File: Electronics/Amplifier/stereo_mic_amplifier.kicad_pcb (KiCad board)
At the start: 2 copper layers, 26 parts, among them P1 mic_L, P2 mic_R, P3 batt, P4 CONN_01X03, U1 TL072

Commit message: Fixed dual potentiometer pins
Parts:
- moved C1 217.8 mm to (-87.6, 106.7)
- moved R8 211.6 mm to (-108.0, 125.7)
- moved C2 203.9 mm to (-77.5, 83.8)
- moved C5 186.3 mm to (-69.8, 40.6)
- moved C8 184.6 mm to (229.9, 111.8), turned to 180 degrees
- moved C3 184.5 mm to (229.9, 95.2), turned to 270 degrees
- moved C4 177.8 mm to (-66.0, 58.4)
- moved P4 174.1 mm to (-100.3, 27.9), turned to 270 degrees
- moved C7 171.5 mm to (257.8, 87.6), turned to 270 degrees
- moved U1 156.9 mm to (250.2, 90.2)
- moved R3 156.5 mm to (237.5, 85.1), turned to 270 degrees
- moved R4 145.3 mm to (240.0, 95.2), turned to 270 degrees
- moved R5 144.9 mm to (241.3, 111.8)
- moved R1 134.9 mm to (-8.89, 57.1)
- moved P2 129.2 mm to (-55.9, 125.7), turned to 270 degrees
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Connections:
- D1 pad 2: Net-(D1-Pad2) -> GND
- P3 pad 1: Net-(D1-Pad2) -> GND
- RV1 pad 11: (no net) -> pot_a_L
- RV1 pad 12: (no net) -> pot_b_L
- RV1 pad 21: (no net) -> pot_a_R
- RV1 pad 22: (no net) -> pot_b_R

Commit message: Deciding layout
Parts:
- moved P4 256.3 mm to (132.1, 135.9)
- moved C1 191.5 mm to (100.3, 69.8), turned to 90 degrees
- moved C3 188.6 mm to (44.5, 129.5)
- moved C2 185.9 mm to (99.1, 142.2), turned to 270 degrees
- moved R8 176.6 mm to (68.6, 121.9), turned to 90 degrees
- moved R6 173.4 mm to (72.4, 108.0), turned to 270 degrees
- moved C7 169.7 mm to (88.4, 97.5), turned to 0 degrees
- moved R5 169.2 mm to (72.4, 121.9), turned to 90 degrees
- moved C8 167.0 mm to (63.2, 123.2), turned to 270 degrees
- moved R4 166.0 mm to (76.2, 121.9)
- moved U1 164.5 mm to (86.4, 105.4)
- moved R3 162.9 mm to (76.2, 108.0)
- moved C9 162.7 mm to (69.8, 97.8)
- moved C5 161.0 mm to (80.8, 97.5)
- moved C4 158.5 mm to (82.8, 113.0)
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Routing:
- net vgnd: track 0.00 -> 28.5 mm
- net +9V: track 0.00 -> 25.8 mm
- net pot_b_R: track 0.00 -> 25.4 mm
- net pot_b_L: track 0.00 -> 17.9 mm
- net GND: track 0.00 -> 17.1 mm
- net Net-(C8-Pad1): track 0.00 -> 11.5 mm
- net L_out: track 0.00 -> 6.39 mm
- net Net-(C9-Pad1): track 0.00 -> 5.61 mm
- net R_out: track 0.00 -> 5.08 mm
- net pot_a_L: track 0.00 -> 4.93 mm
- net pot_a_R: track 0.00 -> 4.83 mm
- net Net-(D2-Pad1): track 0.00 -> 3.81 mm
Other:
- net class Default: clearance 0.2 -> 0.3; trace_width 0.25 -> 0.7; via_dia 0.6 -> 1.6; via_drill 0.4 -> 0.8
- rule trace_clearance: 0.2 -> 0.3

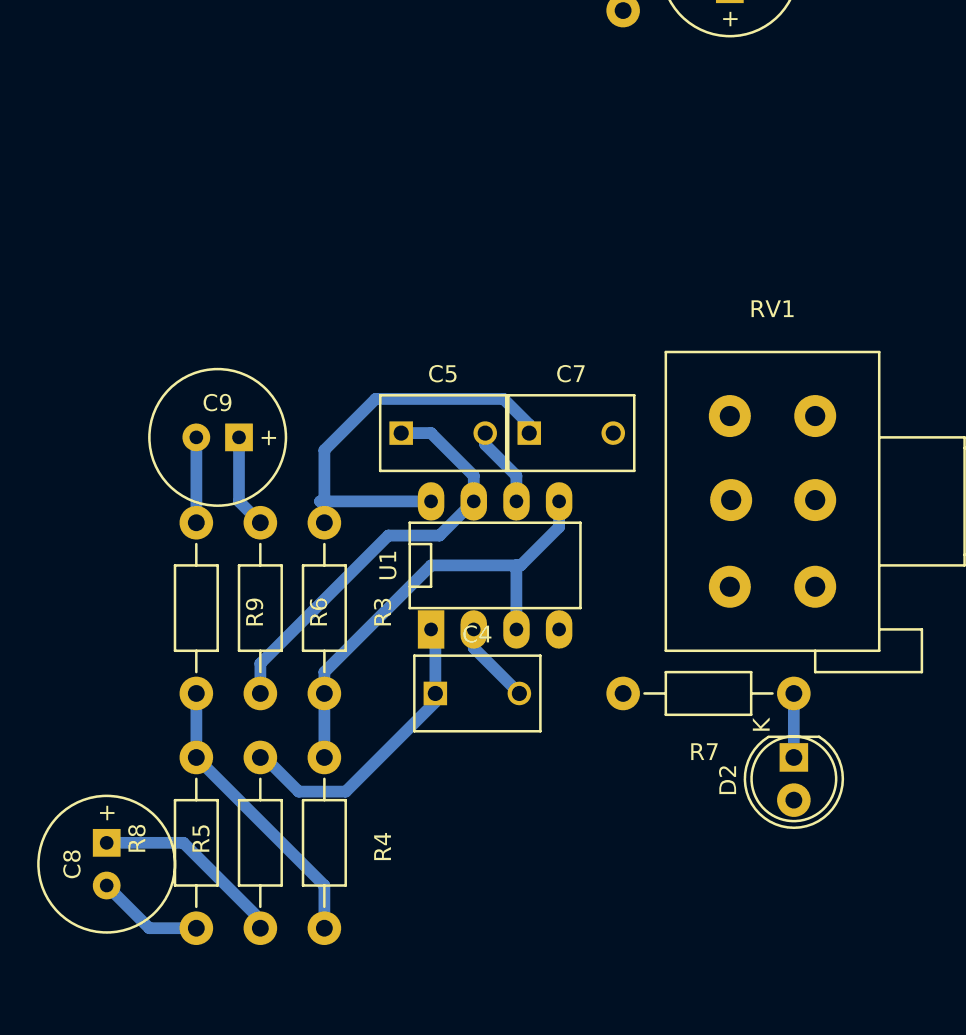
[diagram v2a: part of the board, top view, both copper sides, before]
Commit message: Fixing kicad libraries
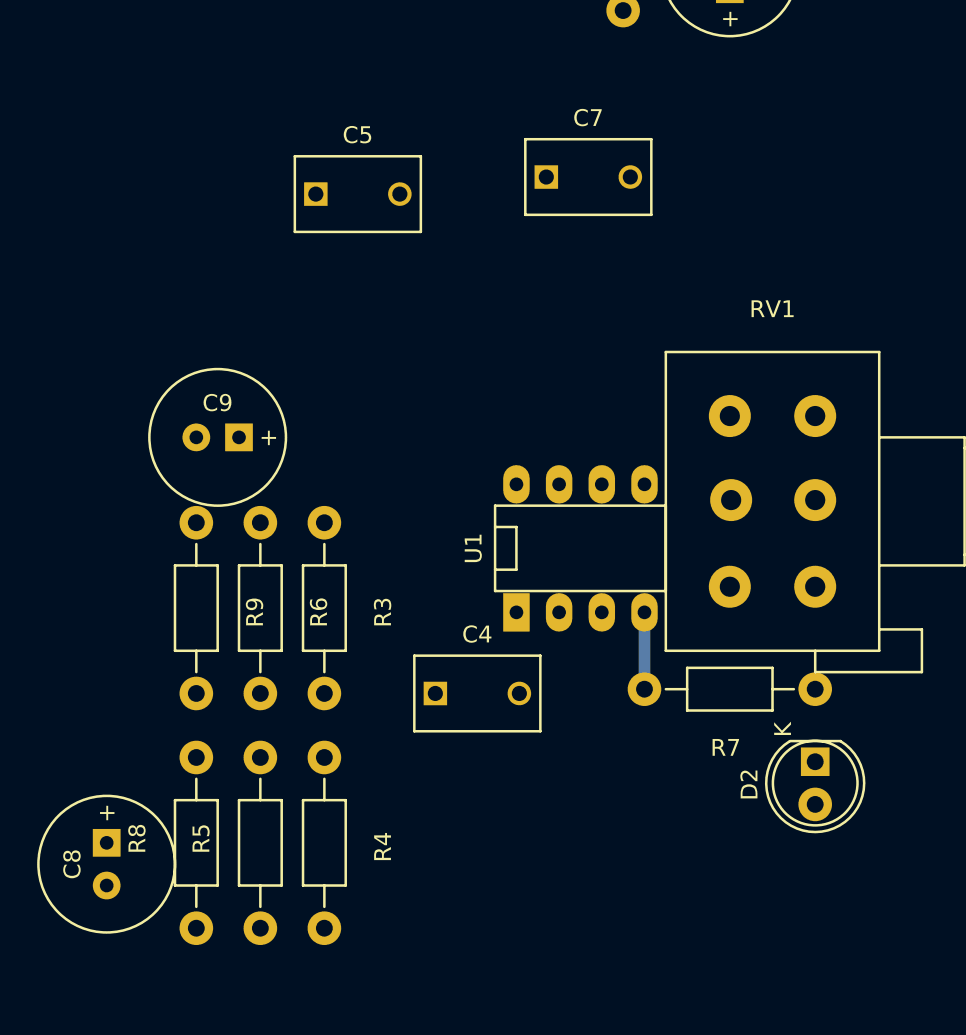
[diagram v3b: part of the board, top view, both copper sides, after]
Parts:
- moved C7 15.3 mm to (89.4, 82.3)
- moved C5 15.1 mm to (75.7, 83.3)
- moved U1 5.18 mm to (91.4, 104.4)
- moved R7 1.30 mm to (100.3, 112.8)
- moved D2 1.30 mm to (105.4, 117.1)
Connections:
- RV1 pad 11: pot_a_L -> (no net)
- RV1 pad 12: pot_b_L -> (no net)
- RV1 pad 21: pot_a_R -> (no net)
- RV1 pad 22: pot_b_R -> (no net)
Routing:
- net vgnd: track 28.5 -> 0.00 mm
- net +9V: track 25.8 -> 0.00 mm
- net pot_b_R: track 25.4 -> 0.00 mm
- net pot_b_L: track 17.9 -> 0.00 mm
- net GND: track 17.1 -> 4.57 mm
- net Net-(C8-Pad1): track 11.5 -> 0.00 mm
- net L_out: track 6.39 -> 0.00 mm
- net Net-(C9-Pad1): track 5.61 -> 0.00 mm
- net R_out: track 5.08 -> 0.00 mm
- net pot_a_L: track 4.93 -> 0.00 mm
- net pot_a_R: track 4.83 -> 0.00 mm
- net Net-(D2-Pad1): track 3.81 -> 0.00 mm
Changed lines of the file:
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@@
 (kicad_pcb (version 4) (host pcbnew "(after 2015-mar-04 BZR unknown)-product")
   (general
-    (links 47)
-    (no_connects 29)
-    (area 27.134999 60.154999 140.388334 151.935001)
+    (links 43)
+    (no_connects 42)
+    (area 0 0 0 0)
     (thickness 1.6)
     (drawings 0)
-    (tracks 50)
+    (tracks 1)
     (zones 0)
     (modules 26)
@@
   )
   (module Capacitors_ThroughHole:C_Disc_D7.5_P5 (layer F.Cu)
-    (at 80.772 97.536)
+    (at 75.692 83.312)
     (descr "Capacitor 7.5mm Disc, Pitch 5mm")
     (tags Capacitor)
@@
   )
   (module Capacitors_ThroughHole:C_Disc_D7.5_P5 (layer F.Cu)
-    (at 88.392 97.536)
+    (at 89.408 82.296)
     (descr "Capacitor 7.5mm Disc, Pitch 5mm")
     (tags Capacitor)
@@
   )
   (module LEDs:LED-5MM (layer F.Cu)
-    (at 104.14 116.84 270)
+    (at 105.41 117.094 270)
     (descr "LED vertical 5mm")
     (tags "LED-5MM LED 5mm")
@@
   )
   (module Resistors_ThroughHole:Resistor_Horizontal_RM10mm (layer F.Cu)
-    (at 99.06 113.03 180)
+    (at 100.33 112.776 180)
     (descr "Resistor, Axial,  RM 10mm, 1/3W,")
     (tags "Resistor, Axial, RM 10mm, 1/3W,")
@@
     (fp_line (start 3.81 -13.97) (end 3.81 3.81) (layer F.SilkS) (width 0.15))
     (pad 23 thru_hole circle (at -5.08 -10.16) (size 2.49936 2.49936) (drill 1.19888) (layers *.Cu *.Mask F.SilkS))
-    (pad 22 thru_hole circle (at -5.00126 -5.15874) (size 2.49936 2.49936) (drill 1.19888) (layers *.Cu *.Mask F.SilkS)
-      (net 8 pot_b_R))
-    (pad 21 thru_hole circle (at -5.08 0) (size 2.49936 2.49936) (drill 1.19888) (layers *.Cu *.Mask F.SilkS)
-      (net 4 pot_a_R))
-    (pad 12 thru_hole circle (at 0 -5.15874) (size 2.49936 2.49936) (drill 1.19888) (layers *.Cu *.Mask F.SilkS)
-      (net 7 pot_b_L))
+    (pad 22 thru_hole circle (at -5.00126 -5.15874) (size 2.49936 2.49936) (drill 1.19888) (layers *.Cu *.Mask F.SilkS))
+    (pad 21 thru_hole circle (at -5.08 0) (size 2.49936 2.49936) (drill 1.19888) (layers *.Cu *.Mask F.SilkS))
+    (pad 12 thru_hole circle (at 0 -5.15874) (size 2.49936 2.49936) (drill 1.19888) (layers *.Cu *.Mask F.SilkS))
     (pad 13 thru_hole circle (at 0 -10.16) (size 2.49936 2.49936) (drill 1.19888) (layers *.Cu *.Mask F.SilkS))
-    (pad 11 thru_hole circle (at 0 0) (size 2.49936 2.49936) (drill 1.19888) (layers *.Cu *.Mask F.SilkS)
-      (net 2 pot_a_L))
+    (pad 11 thru_hole circle (at 0 0) (size 2.49936 2.49936) (drill 1.19888) (layers *.Cu *.Mask F.SilkS))
     (model Potentiometers.3dshapes/Potentiometer_Alps-RK163-double_15mm.wrl
       (at (xyz 0 0 0))
@@
   )
   (module Sockets_DIP:DIP-8__300_ELL (layer F.Cu)
-    (at 86.36 105.41)
+    (at 91.44 104.394)
     (descr "8 pins DIL package, elliptical pads")
     (tags DIL)
@@
     )
   )
-  (segment (start 85.09 109.22) (end 85.09 110.316) (width 0.7) (layer B.Cu) (net 2))
-  (segment (start 85.09 110.316) (end 87.804 113.03) (width 0.7) (layer B.Cu) (net 2))
-  (segment (start 85.772 97.536) (end 85.772 98.218) (width 0.7) (layer B.Cu) (net 4))
-  (segment (start 85.772 98.218) (end 87.63 100.076) (width 0.7) (layer B.Cu) (net 4))
-  (segment (start 87.63 100.076) (end 87.63 101.6) (width 0.7) (layer B.Cu) (net 4))
-  (segment (start 76.2 127) (end 76.2 124.46) (width 0.7) (layer B.Cu) (net 5))
-  (segment (start 76.2 124.46) (end 68.58 116.84) (width 0.7) (layer B.Cu) (net 5))
-  (segment (start 68.58 116.84) (end 68.58 113.03) (width 0.7) (layer B.Cu) (net 5))
-  (segment (start 87.63 109.22) (end 87.63 105.41) (width 0.7) (layer B.Cu) (net 6))
-  (segment (start 87.63 105.41) (end 87.63 105.664) (width 0.7) (layer B.Cu) (net 6))
-  (segment (start 87.63 105.664) (end 87.63 105.41) (width 0.7) (layer B.Cu) (net 6))
-  (segment (start 76.2 113.03) (end 76.2 111.76) (width 0.7) (layer B.Cu) (net 6))
-  (segment (start 90.17 103.124) (end 90.17 101.6) (width 0.7) (layer B.Cu) (net 6))
-  (segment (start 87.884 105.41) (end 90.17 103.124) (width 0.7) (layer B.Cu) (net 6))
-  (segment (start 82.55 105.41) (end 87.63 105.41) (width 0.7) (layer B.Cu) (net 6))
-  (segment (start 87.63 105.41) (end 87.884 105.41) (width 0.7) (layer B.Cu) (net 6))
-  (segment (start 76.2 111.76) (end 82.55 105.41) (width 0.7) (layer B.Cu) (net 6))
-  (segment (start 76.2 116.84) (end 76.2 113.03) (width 0.7) (layer B.Cu) (net 6))
-  (segment (start 72.39 116.84) (end 72.644 116.84) (width 0.7) (layer B.Cu) (net 7))
-  (segment (start 72.644 116.84) (end 74.676 118.872) (width 0.7) (layer B.Cu) (net 7))
-  (segment (start 74.676 118.872) (end 77.47 118.872) (width 0.7) (layer B.Cu) (net 7))
-  (segment (start 77.47 118.872) (end 82.804 113.538) (width 0.7) (layer B.Cu) (net 7))
-  (segment (start 82.804 113.538) (end 82.804 113.03) (width 0.7) (layer B.Cu) (net 7))
-  (segment (start 82.804 113.03) (end 82.804 109.474) (width 0.7) (layer B.Cu) (net 7))
-  (segment (start 82.804 109.474) (end 82.55 109.22) (width 0.7) (layer B.Cu) (net 7))
-  (segment (start 72.39 113.03) (end 72.39 111.252) (width 0.7) (layer B.Cu) (net 8))
-  (segment (start 83.058 103.632) (end 85.09 101.6) (width 0.7) (layer B.Cu) (net 8))
-  (segment (start 80.01 103.632) (end 83.058 103.632) (width 0.7) (layer B.Cu) (net 8))
-  (segment (start 72.39 111.252) (end 80.01 103.632) (width 0.7) (layer B.Cu) (net 8))
-  (segment (start 85.09 101.6) (end 85.09 100.076) (width 0.7) (layer B.Cu) (net 8))
-  (segment (start 82.55 97.536) (end 80.772 97.536) (width 0.7) (layer B.Cu) (net 8))
-  (segment (start 85.09 100.076) (end 82.55 97.536) (width 0.7) (layer B.Cu) (net 8))
-  (segment (start 82.55 101.6) (end 76.2 101.6) (width 0.7) (layer B.Cu) (net 9))
-  (segment (start 76.2 101.6) (end 75.946 101.6) (width 0.7) (layer B.Cu) (net 9))
-  (segment (start 75.946 101.6) (end 76.2 101.6) (width 0.7) (layer B.Cu) (net 9))
-  (segment (start 88.392 97.536) (end 88.392 97.028) (width 0.7) (layer B.Cu) (net 9))
-  (segment (start 88.392 97.028) (end 86.868 95.504) (width 0.7) (layer B.Cu) (net 9))
-  (segment (start 86.868 95.504) (end 79.248 95.504) (width 0.7) (layer B.Cu) (net 9))
-  (segment (start 79.248 95.504) (end 76.2 98.552) (width 0.7) (layer B.Cu) (net 9))
-  (segment (start 76.2 98.552) (end 76.2 101.6) (width 0.7) (layer B.Cu) (net 9))
-  (segment (start 76.2 101.6) (end 76.2 102.87) (width 0.7) (layer B.Cu) (net 9))
-  (segment (start 68.58 127) (end 65.786 127) (width 0.7) (layer B.Cu) (net 10) (status 400000))
-  (segment (start 65.786 127) (end 63.246 124.46) (width 0.7) (layer B.Cu) (net 10) (status 800000))
-  (segment (start 72.39 127) (end 72.39 126.492) (width 0.7) (layer B.Cu) (net 11) (status C00000))
-  (segment (start 72.39 126.492) (end 67.818 121.92) (width 0.7) (layer B.Cu) (net 11) (status 400000))
-  (segment (start 67.818 121.92) (end 63.246 121.92) (width 0.7) (layer B.Cu) (net 11) (status 800000))
-  (segment (start 68.58 102.87) (end 68.58 97.79) (width 0.7) (layer B.Cu) (net 12))
-  (segment (start 71.12 97.79) (end 71.12 101.6) (width 0.7) (layer B.Cu) (net 13))
-  (segment (start 71.12 101.6) (end 72.39 102.87) (width 0.7) (layer B.Cu) (net 13))
-  (segment (start 104.14 116.83866) (end 104.14 113.03) (width 0.7) (layer B.Cu) (net 14))
+  (segment (start 95.25 108.204) (end 95.25 112.776) (width 0.7) (layer B.Cu) (net 5))
 )

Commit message: Work on the layout
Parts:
- RV1: value Dual A100K -> DUAL_POT_OK
- moved C8 74.8 mm to (138.0, 120.7)
- moved R8 66.1 mm to (134.5, 127.0), turned to 180 degrees
- moved C9 64.6 mm to (120.8, 137.5), turned to 0 degrees
- moved R9 60.7 mm to (124.7, 131.1), turned to 0 degrees
- moved R5 49.2 mm to (121.2, 115.6)
- moved P3 48.1 mm to (75.7, 121.4), turned to 90 degrees
- moved R6 47.5 mm to (112.6, 133.1), turned to 90 degrees
- moved D1 43.8 mm to (76.8, 118.2), turned to 0 degrees
- moved C3 41.1 mm to (77.3, 104.9), turned to 180 degrees
- moved R1 39.8 mm to (81.9, 105.3)
- moved C6 37.0 mm to (77.3, 112.5), turned to 180 degrees
- moved C1 35.8 mm to (77.3, 97.3), turned to 180 degrees
- moved P1 34.4 mm to (86.5, 93.7)
- moved C7 34.0 mm to (86.9, 116.2), turned to 90 degrees
- moved C5 32.3 mm to (91.9, 111.3), turned to 270 degrees
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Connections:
- D2 pad 1: Net-(D2-Pad1) -> GND
- D2 pad 2: +9V -> Net-(D2-Pad2)
- R7 pad 1: Net-(D2-Pad1) -> +9V
- R7 pad 2: GND -> Net-(D2-Pad2)
- RV1 pad 12: (no net) -> pot_b_L
- RV1 pad 13: (no net) -> pot_a_L
- RV1 pad 22: (no net) -> pot_b_R
- RV1 pad 23: (no net) -> pot_a_R
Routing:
- net +9V: track 0.00 -> 60.4 mm
- net GND: track 4.57 -> 56.1 mm
- net pot_a_L: track 0.00 -> 40.0 mm
- net pot_a_R: track 0.00 -> 34.9 mm
- net vgnd: track 0.00 -> 21.7 mm
- net pot_b_L: track 0.00 -> 20.6 mm
- net pot_b_R: track 0.00 -> 17.4 mm
- net Net-(C1-Pad2): track 0.00 -> 15.7 mm
- net Net-(C2-Pad2): track 0.00 -> 12.6 mm
- net Net-(D2-Pad2): track 0.00 -> 4.83 mm

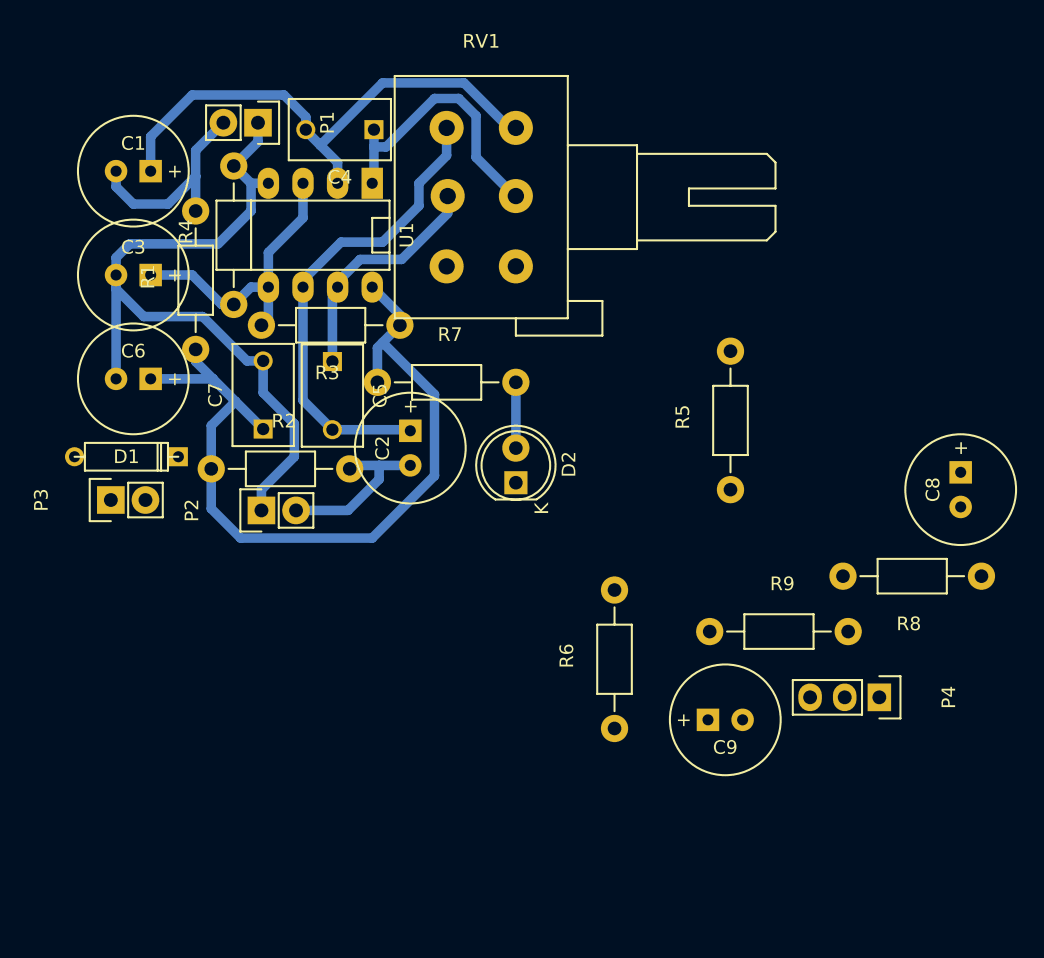
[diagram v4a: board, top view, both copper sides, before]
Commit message: Increased pad sizes & improvements in layout
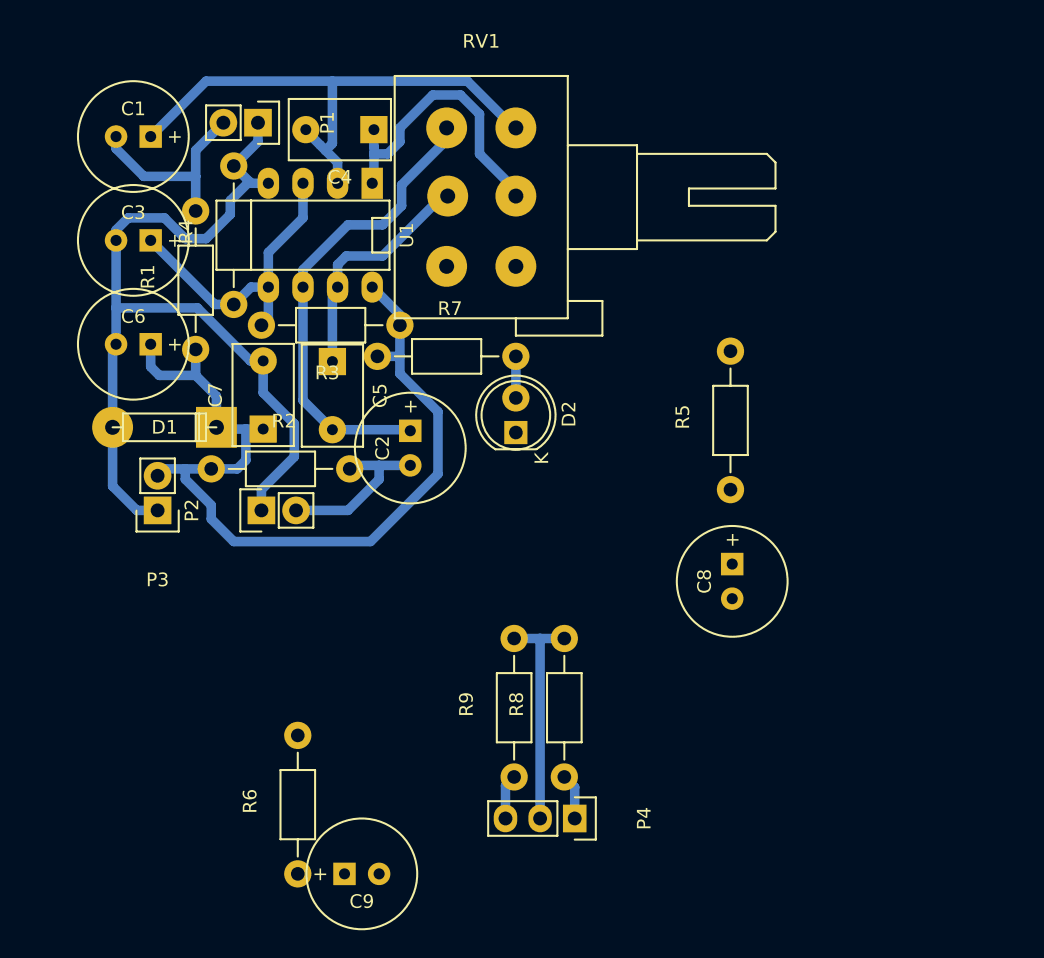
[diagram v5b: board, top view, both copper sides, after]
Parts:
- moved C9 29.0 mm to (94.1, 148.8)
- moved R8 27.3 mm to (109.0, 136.7), turned to 90 degrees
- moved R6 25.6 mm to (89.4, 143.8)
- moved P4 24.1 mm to (109.7, 144.8)
- moved R9 20.2 mm to (105.3, 136.7), turned to 90 degrees
- moved C8 18.1 mm to (121.3, 127.4)
- moved D2 3.68 mm to (105.4, 116.5)
- moved D1 3.53 mm to (79.6, 116.1)
- moved P3 3.51 mm to (79.1, 122.2), turned to 180 degrees
- moved C3 2.54 mm to (77.3, 102.4)
- moved C6 2.54 mm to (77.3, 110.0)
- moved C1 2.54 mm to (77.3, 94.7)
- moved R7 1.91 mm to (100.3, 110.9)
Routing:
- net GND: track 56.1 -> 85.2 mm
- net +9V: track 60.4 -> 65.5 mm
- net L_out: track 0.00 -> 3.36 mm
- net R_out: track 0.00 -> 3.31 mm
- net vgnd: track 21.7 -> 23.7 mm
- net Net-(D2-Pad2): track 4.83 -> 3.05 mm
- net pot_b_L: track 20.6 -> 21.9 mm
- net Net-(C1-Pad2): track 15.7 -> 14.9 mm

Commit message: backup
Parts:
- moved R5 44.9 mm to (83.2, 139.6)
- moved C8 41.6 mm to (89.3, 153.9)
- moved R6 29.4 mm to (60.2, 146.9)
- moved C9 22.5 mm to (71.8, 151.8)
- moved P4 19.5 mm to (105.7, 125.7), turned to 0 degrees
- moved R8 15.3 mm to (97.5, 126.5), turned to 180 degrees
- moved R9 10.1 mm to (97.5, 130.2), turned to 180 degrees
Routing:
- net pot_b_L: track 21.9 -> 40.0 mm
- net pot_b_R: track 17.8 -> 33.3 mm
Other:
- board outline added: 34.2 x 45.3 mm

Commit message: Layout progress
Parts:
- R5, R6, R8, R9: footprint Resistors_ThroughHole:Resistor_Horizontal_RM10mm -> Resistors_ThroughHole:Resistor_Vertical_RM5mm
- moved R6 50.1 mm to (102.0, 119.4)
- moved C9 36.7 mm to (96.9, 125.1), turned to 180 degrees
- moved C8 24.7 mm to (90.6, 129.3), turned to 180 degrees
- moved R5 24.1 mm to (104.5, 128.4), turned to 270 degrees
- moved R8 17.3 mm to (80.6, 130.0)
- moved R9 17.1 mm to (80.7, 127.3), turned to 0 degrees
- moved P4 10.5 mm to (96.4, 130.6), turned to 90 degrees
- moved P3 2.75 mm to (77.6, 119.9), turned to 90 degrees
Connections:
- R5 pad 1: Net-(C8-Pad1) -> pot_b_L
- R5 pad 2: pot_b_L -> Net-(C8-Pad1)
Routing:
- net GND: track 85.2 -> 111.8 mm
- net pot_b_L: track 40.0 -> 52.0 mm
- net L_out: track 3.36 -> 0.00 mm
- net R_out: track 3.31 -> 0.00 mm
- net +9V: track 65.5 -> 64.5 mm
- net pot_b_R: track 33.3 -> 34.2 mm
